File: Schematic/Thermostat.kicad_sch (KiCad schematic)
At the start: 42 parts, among them J1 Relay conn., J2 Thermocouple, J4 USB_B_Micro, J5 Firmware, K1 SONGLE_SRD_05VDC_SL_C, Q1 BSS138, SW1 Reset, SW2 Temp+, SW3 Temp-, SW4 Preset1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

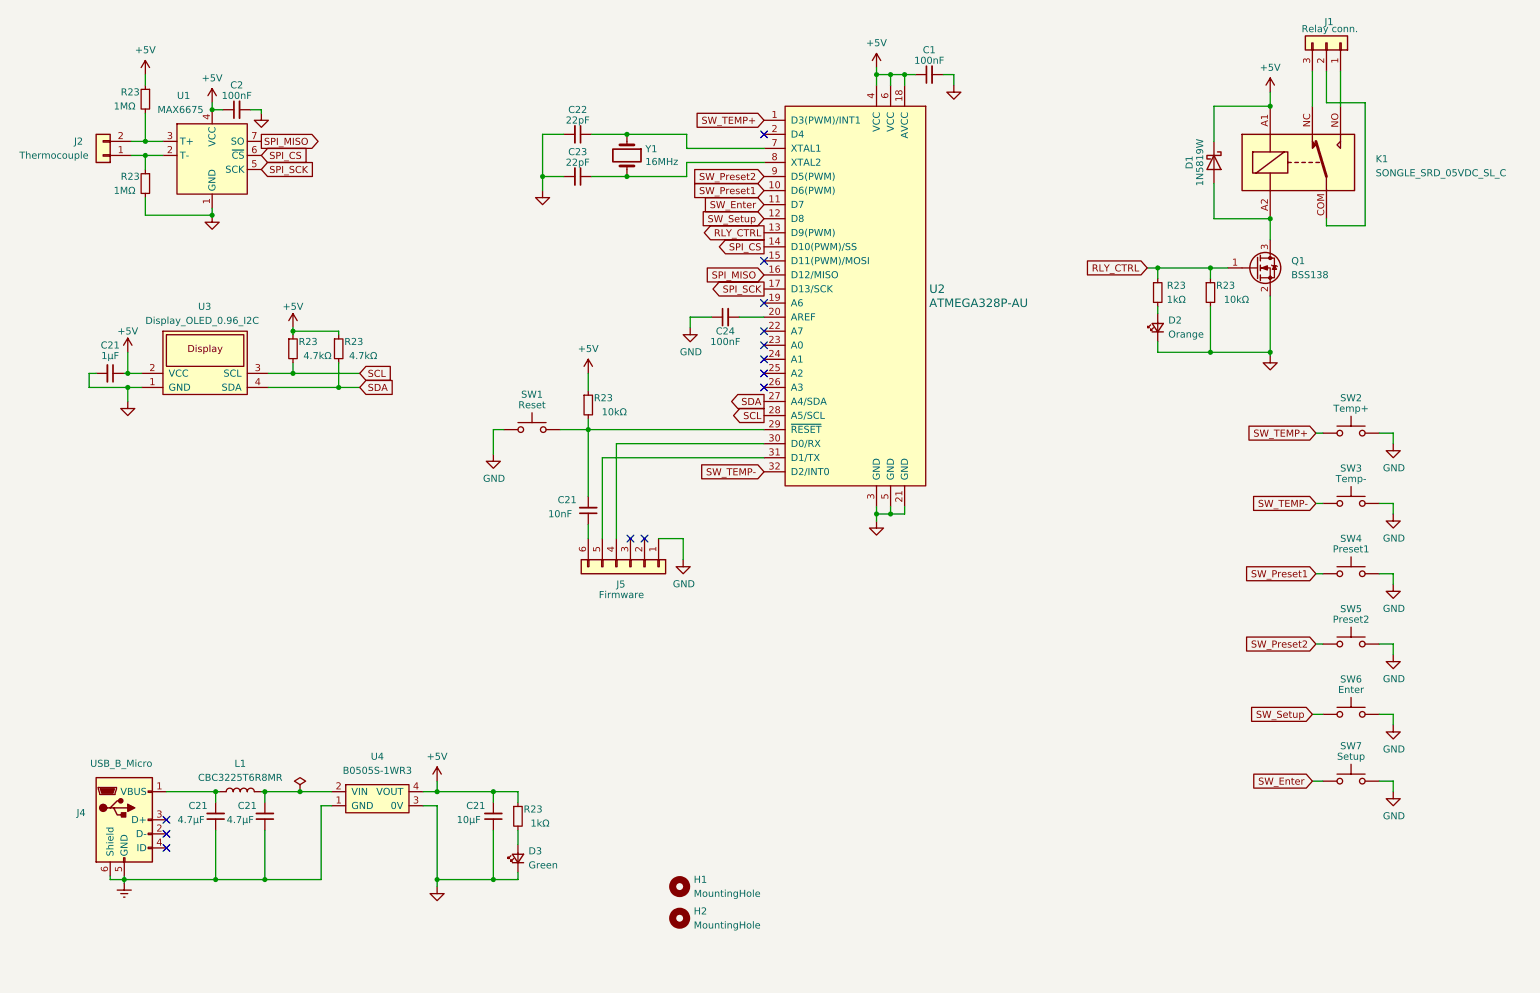
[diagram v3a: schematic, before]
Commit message: Added status LEDs, rearranged buttons
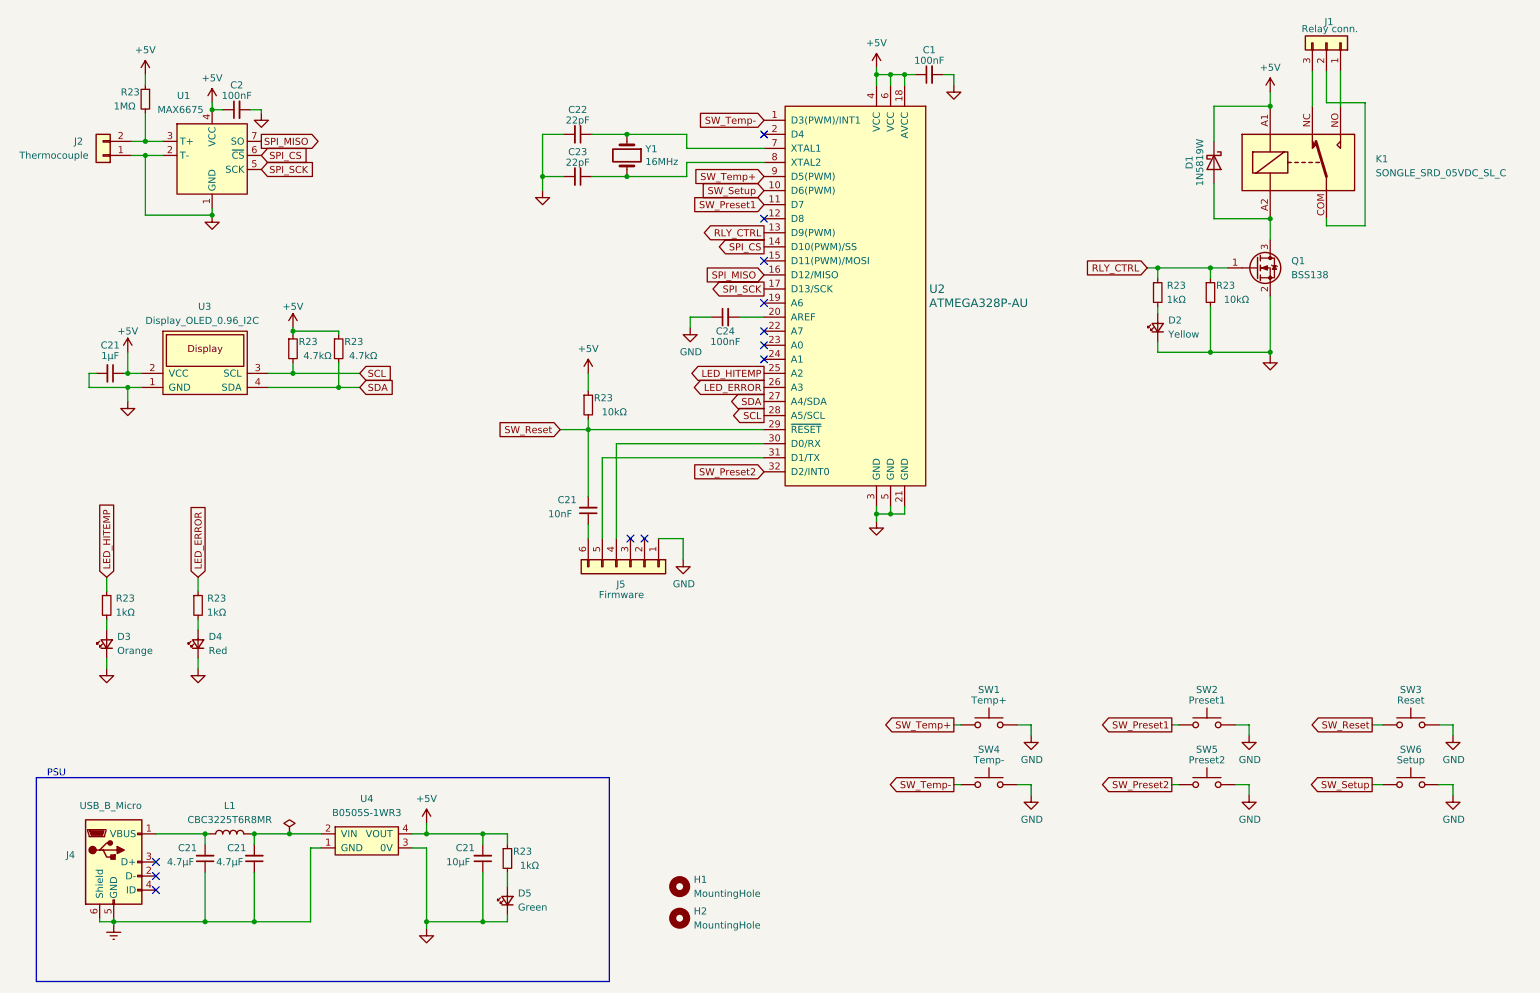
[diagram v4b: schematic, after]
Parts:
- removed R23: 1MΩ, Resistor_SMD:R_0603_1608Metric_Pad0.98x0.95mm_HandSolder, symbol Device:R_Small
- removed SW1: Reset, Retronics_Switches:AlpsAlpine_SKQYPCE010, symbol Switch:SW_Push
- added D3: Orange, LED_SMD:LED_0603_1608Metric_Pad1.05x0.95mm_HandSolder, symbol Device:LED_Small
- added D4: Red, LED_SMD:LED_0603_1608Metric_Pad1.05x0.95mm_HandSolder, symbol Device:LED_Small
- added R23 (x2): 1kΩ, Resistor_SMD:R_0603_1608Metric_Pad0.98x0.95mm_HandSolder, symbol Device:R_Small
- D2: value Orange -> Yellow
- SW3: renamed from SW6; value Enter -> Reset
- renumbered D3 to D5, SW2 to SW1, SW4 to SW2, SW3 to SW4, SW7 to SW6
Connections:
- net GND: now also J2.1 (Pin_1), U1.2 (T-), D3.1 (K), D4.1 (K)
- net SW_Preset1: now also U2.11 (D7); no longer U2.10 (D6(PWM))
- net SW_Preset2: now also U2.32 (D2/INT0); no longer U2.9 (D5(PWM))
- net SW_Setup: now also SW6.1, U2.10 (D6(PWM)); no longer SW3.1, U2.12 (D8)
- net SW_Reset: now reaches C21.2, R23.2, U2.29 (~{RESET})
- net SW_Reset: now also SW3.1
- net LED_HITEMP: now reaches U2.25 (A2)
- net LED_HITEMP: now also R23.1
- net LED_ERROR: now reaches U2.26 (A3)
- net LED_ERROR: now also R23.1
- removed net SW_Enter: SW6.1, U2.11 (D7)
- net SW_TEMP+ renamed SW_Temp+
- net SW_Temp+: now also U2.9 (D5(PWM)); no longer U2.1 (D3(PWM)/INT1)
- net SW_TEMP- renamed SW_Temp-
- net SW_Temp-: now also U2.1 (D3(PWM)/INT1); no longer U2.32 (D2/INT0)
- new net: D4.2 (A), R23.2
- new net: D3.2 (A), R23.2
- no-connect marks 13 -> 12
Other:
- note added: "PSU"
- company: (none) -> Retronics - Bjørner Sandom
- title: (none) -> Programmable Thermostat
- moved on the sheet: C21, D5, J4, L1, R23, SW1, SW2, SW3, SW4, SW5, SW6, U4
